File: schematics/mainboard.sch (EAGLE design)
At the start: 146 parts, among them IC1 TEENSY 3.6, IC10 UDN2981A, IC2 LM393, IC3 DRV8835, IC4 LM2596S-ADJ, IC5 LM2596S-5.0, IC6 PCF8574P, IC7 PCF8574P, IC8 LD1117A, IC9 TSOP34830, J1 Servo_1, J10 Uart_5, J11 Servo_3, J12 USB_Host, J13 BNO055, J14 I2C_2, J15 SPI_Display, J16 SPI_2, J17 Uart_6, J18 Maus_select, J19 Erw_analog, J2 Servo_2, J20 Erw_PWM, J21 Erw_GPIO, J22 GY-271, J23 Uart_1, J24 I2C_3, J3 Erw_Pow, J30 H-Bridge Mode, J4 Uart_2, J5 BPS, J6 Erw_ENA, J7 I2C_0, J8 I2C_Display, J9 RPI_SPI0, Q2 IRL3103, SW1 TL36WO, U1 CNY70, U2 BLE-HM-10, U3 BSS138, U4 BSS138, U5 BSS138, X1 Bat

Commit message: Servo PWM pullups corrected, battery voltage divider adjusted
schematic layout improved, signal names unified
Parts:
- J19: device pinhead_ts:PINHD-1X3 -> pinhead_ts:PINHD-1X2
- R1, R37, R38: value 10k -> 4k7
- R2: value 82k -> 100k
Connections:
- net POW4 renamed PWR_SERVO
- net PWM0 renamed PWM1
- net V_BAT_FB renamed BAT_IN_FB
- net +3V3: now also R1.1; no longer R1.2
- net PWM3: now also R1.2; no longer R1.1
- net SERVO3_FB: no longer J19.3
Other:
- note added: "max. 18V Eingangsspannung!"
- note removed: "PWM Pullups erforderlich?"
- moved on the sheet: C16, C17, D3, IC2A, IC2B, J1, J20, R1, R19, R20, R28, R34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

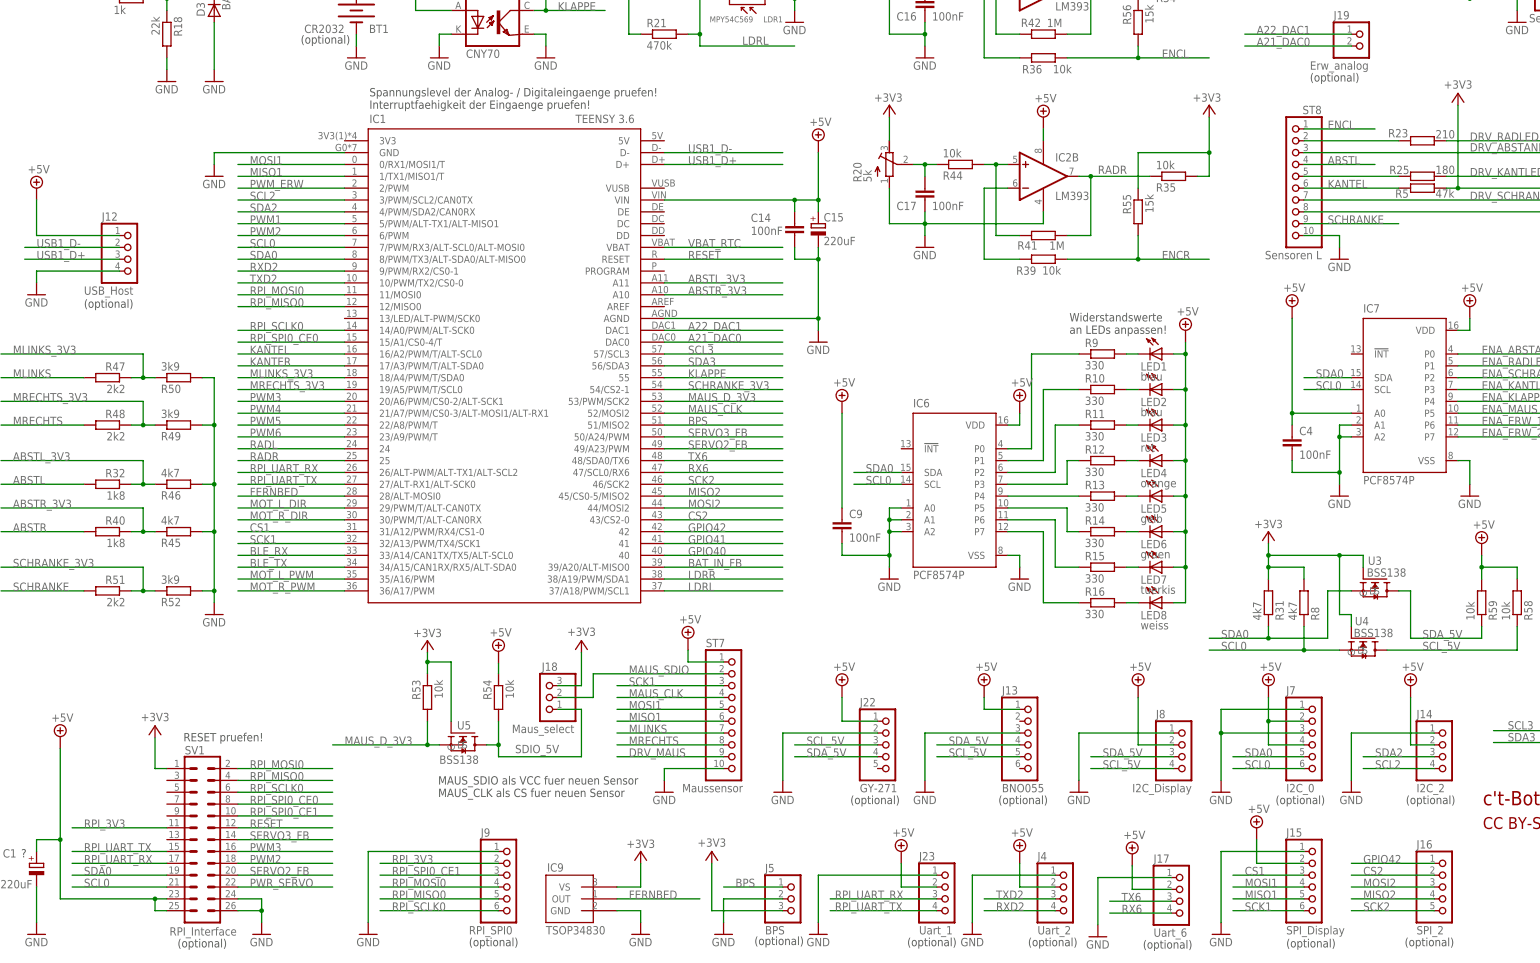
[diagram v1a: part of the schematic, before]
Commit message: bugfix for i2c bus mapping on mainboard
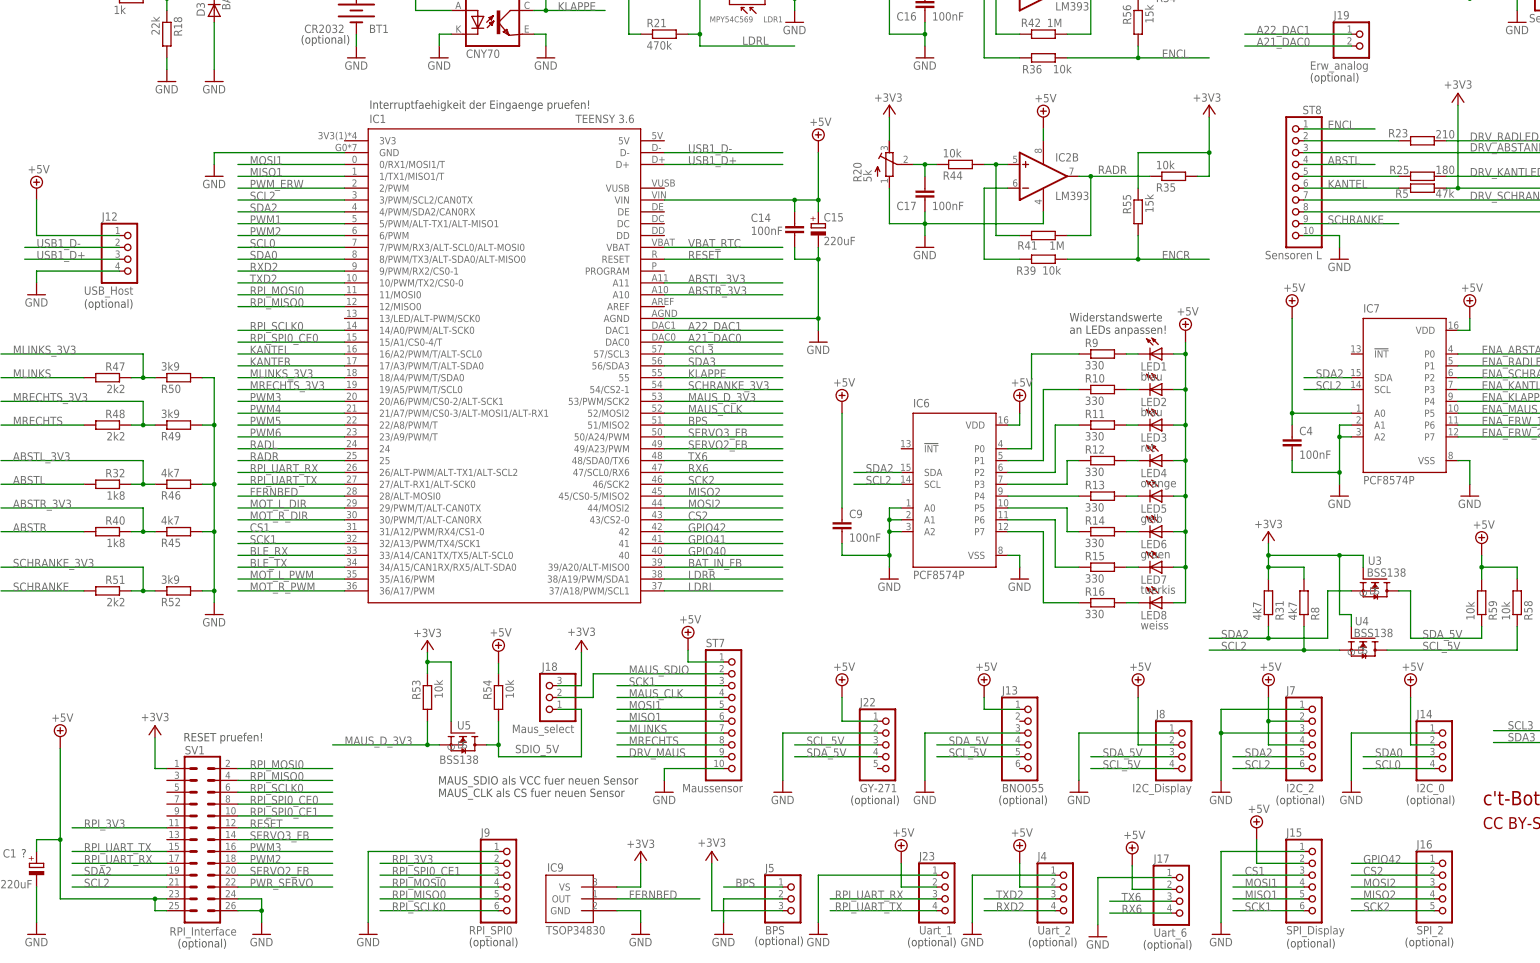
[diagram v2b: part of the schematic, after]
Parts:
- J14: value I2C_2 -> I2C_0
- J7: value I2C_0 -> I2C_2
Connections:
- net SCL0: now also J14.4; no longer IC6.SCL, IC7.SCL, J7.6, R8.1, SV1.21, U4.S
- net SCL2: now also IC6.SCL, IC7.SCL, J7.6, R8.1, SV1.21, U4.S; no longer J14.4
- net SDA0: now also J14.3; no longer IC6.SDA, IC7.SDA, J7.5, R31.1, SV1.19, U3.S
- net SDA2: now also IC6.SDA, IC7.SDA, J7.5, R31.1, SV1.19, U3.S; no longer J14.3
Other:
- note added: "Interruptfaehigkeit der Eingaenge pruefen!"
- note removed: "Spannungslevel der Analog- / Digitaleingaenge pruefen! Interruptfaehigkeit der Eingaenge pruefen!"
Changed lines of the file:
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@@
 <?xml version="1.0" encoding="utf-8"?>
 <!DOCTYPE eagle SYSTEM "eagle.dtd">
-<eagle version="8.6.3">
+<eagle version="8.7.0">
 <drawing>
 <settings>
@@
 <part name="GND20" library="supply1" library_urn="urn:adsk.eagle:library:371" deviceset="GND" device=""/>
 <part name="SUPPLY22" library="supply2_ts" deviceset="+5V" device="" value="+5V"/>
-<part name="J7" library="pinhead_ts" deviceset="PINHD-1X6" device="" value="I2C_0"/>
+<part name="J7" library="pinhead_ts" deviceset="PINHD-1X6" device="" value="I2C_2"/>
 <part name="SUPPLY26" library="supply2_ts" deviceset="+5V" device="" value="+5V"/>
 <part name="GND45" library="supply1" library_urn="urn:adsk.eagle:library:371" deviceset="GND" device=""/>
@@
 <part name="J11" library="pinhead_ts" deviceset="PINHD-1X4" device="" value="Servo_3"/>
 <part name="GND44" library="supply1" library_urn="urn:adsk.eagle:library:371" deviceset="GND" device=""/>
-<part name="J14" library="pinhead_ts" deviceset="PINHD-1X4" device="" value="I2C_2"/>
+<part name="J14" library="pinhead_ts" deviceset="PINHD-1X4" device="" value="I2C_0"/>
 <part name="J15" library="pinhead_ts" deviceset="PINHD-1X6" device="" value="SPI_Display"/>
 <part name="GND46" library="supply1" library_urn="urn:adsk.eagle:library:371" deviceset="GND" device=""/>
@@
 <text x="320.294" y="32.766" size="3.048" layer="94">c't-Bot Hauptplatine v2     !!! UNTESTED DRAFT !!!</text>
 <text x="408.178" y="9.906" size="2.54" layer="94" font="vector">0.2</text>
-<text x="81.534" y="182.118" size="1.778" layer="97">Spannungslevel der Analog- / Digitaleingaenge pruefen!
-Interruptfaehigkeit der Eingaenge pruefen!</text>
+<text x="81.534" y="182.118" size="1.778" layer="97">Interruptfaehigkeit der Eingaenge pruefen!</text>
 <text x="214.63" y="216.408" size="1.778" layer="97">Schaltung checken!
 Widerstandswerte pruefen!</text>
@@
 </segment>
 </net>
-<net name="SDA0" class="0">
+<net name="SDA2" class="0">
 <segment>
 <pinref part="IC7" gate="G$1" pin="SDA"/>
@@
 </segment>
 <segment>
-<pinref part="IC1" gate="G$1" pin="8/PWM/TX3/ALT-SDA0/ALT-MISO0"/>
-<wire x1="76.2" y1="149.86" x2="53.34" y2="149.86" width="0.1524" layer="91"/>
-<label x="55.88" y="149.86" size="1.778" layer="95"/>
+<pinref part="IC1" gate="G$1" pin="4/PWM/SDA2/CAN0RX"/>
+<wire x1="76.2" y1="160.02" x2="53.34" y2="160.02" width="0.1524" layer="91"/>
+<label x="55.88" y="160.02" size="1.778" layer="95"/>
 </segment>
 </net>
-<net name="SCL0" class="0">
+<net name="SCL2" class="0">
 <segment>
 <pinref part="IC7" gate="G$1" pin="SCL"/>
@@
 </segment>
 <segment>
-<pinref part="IC1" gate="G$1" pin="7/PWM/RX3/ALT-SCL0/ALT-MOSI0"/>
-<wire x1="76.2" y1="152.4" x2="53.34" y2="152.4" width="0.1524" layer="91"/>
-<label x="55.88" y="152.4" size="1.778" layer="95"/>
+<pinref part="IC1" gate="G$1" pin="3/PWM/SCL2/CAN0TX"/>
+<wire x1="76.2" y1="162.56" x2="53.34" y2="162.56" width="0.1524" layer="91"/>
+<label x="55.88" y="162.56" size="1.778" layer="95"/>
 </segment>
 </net>
@@
 </segment>
 </net>
-<net name="SCL2" class="0">
-<segment>
-<pinref part="J14" gate="A" pin="4"/>
-<wire x1="294.64" y1="40.64" x2="309.88" y2="40.64" width="0.1524" layer="91"/>
-<label x="297.18" y="40.64" size="1.778" layer="95"/>
-</segment>
-<segment>
-<pinref part="IC1" gate="G$1" pin="3/PWM/SCL2/CAN0TX"/>
-<wire x1="76.2" y1="162.56" x2="53.34" y2="162.56" width="0.1524" layer="91"/>
-<label x="55.88" y="162.56" size="1.778" layer="95"/>
-</segment>
-</net>
-<net name="SDA2" class="0">
-<segment>
-<pinref part="J14" gate="A" pin="3"/>
-<wire x1="294.64" y1="43.18" x2="309.88" y2="43.18" width="0.1524" layer="91"/>
-<label x="297.18" y="43.18" size="1.778" layer="95"/>
-</segment>
-<segment>
-<pinref part="IC1" gate="G$1" pin="4/PWM/SDA2/CAN0RX"/>
-<wire x1="76.2" y1="160.02" x2="53.34" y2="160.02" width="0.1524" layer="91"/>
-<label x="55.88" y="160.02" size="1.778" layer="95"/>
-</segment>
-</net>
 <net name="PWM4" class="0">
 <segment>
@@
 </segment>
 </net>
+<net name="SCL0" class="0">
+<segment>
+<pinref part="IC1" gate="G$1" pin="7/PWM/RX3/ALT-SCL0/ALT-MOSI0"/>
+<wire x1="76.2" y1="152.4" x2="53.34" y2="152.4" width="0.1524" layer="91"/>
+<label x="55.88" y="152.4" size="1.778" layer="95"/>
+</segment>
+<segment>
+<pinref part="J14" gate="A" pin="4"/>
+<wire x1="294.64" y1="40.64" x2="309.88" y2="40.64" width="0.1524" layer="91"/>
+<label x="297.18" y="40.64" size="1.778" layer="95"/>
+</segment>
+</net>
+<net name="SDA0" class="0">
+<segment>
+<pinref part="IC1" gate="G$1" pin="8/PWM/TX3/ALT-SDA0/ALT-MISO0"/>
+<wire x1="76.2" y1="149.86" x2="53.34" y2="149.86" width="0.1524" layer="91"/>
+<label x="55.88" y="149.86" size="1.778" layer="95"/>
+</segment>
+<segment>
+<pinref part="J14" gate="A" pin="3"/>
+<wire x1="294.64" y1="43.18" x2="309.88" y2="43.18" width="0.1524" layer="91"/>
+<label x="297.18" y="43.18" size="1.778" layer="95"/>
+</segment>
+</net>

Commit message: schematics updated to rev 0.3
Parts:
- removed J22: GY-271, pinhead_ts:PINHD-1X5
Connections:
- net RXD2 renamed RX2
- net TXD2 renamed TX2
- net +5V: no longer J22.1
- net GND: no longer J22.2
- net SCL_5V: now also SV1.9; no longer J22.3
- net SDA_5V: now also SV1.7; no longer J22.4
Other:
- note added: "0.3"
- note added: "USB2Bot / WiFi"
- note removed: "0.2"
- moved on the sheet: J13, J14, J24, J7, J8

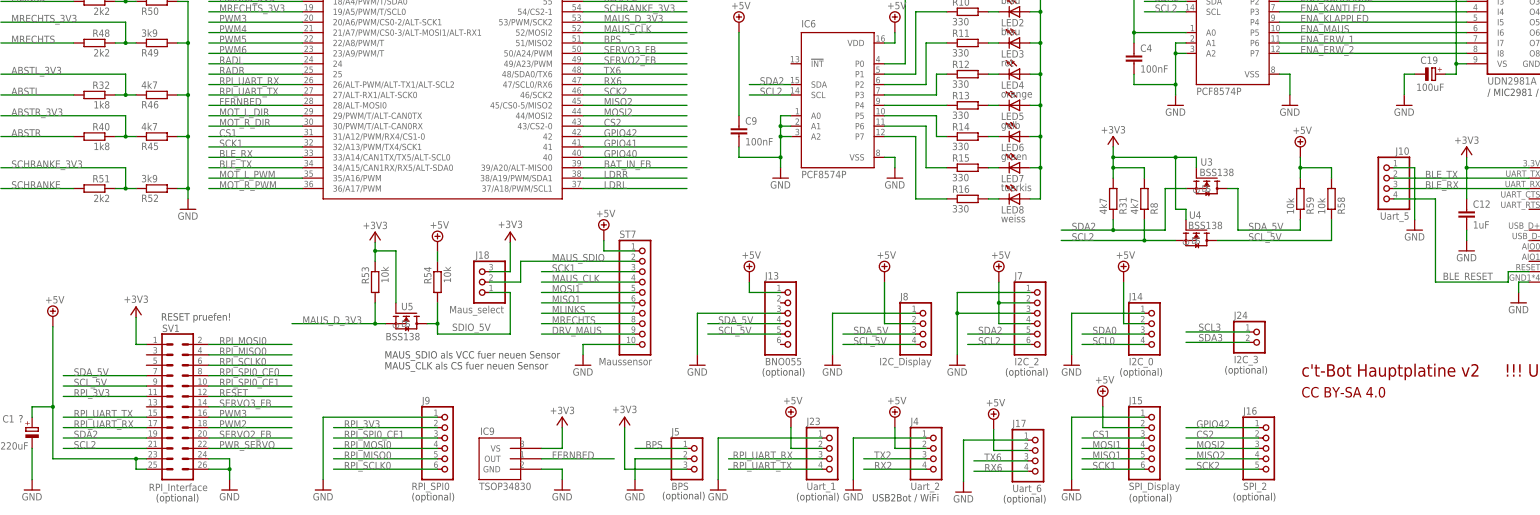
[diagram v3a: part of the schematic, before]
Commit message: mainboard: signal names updated
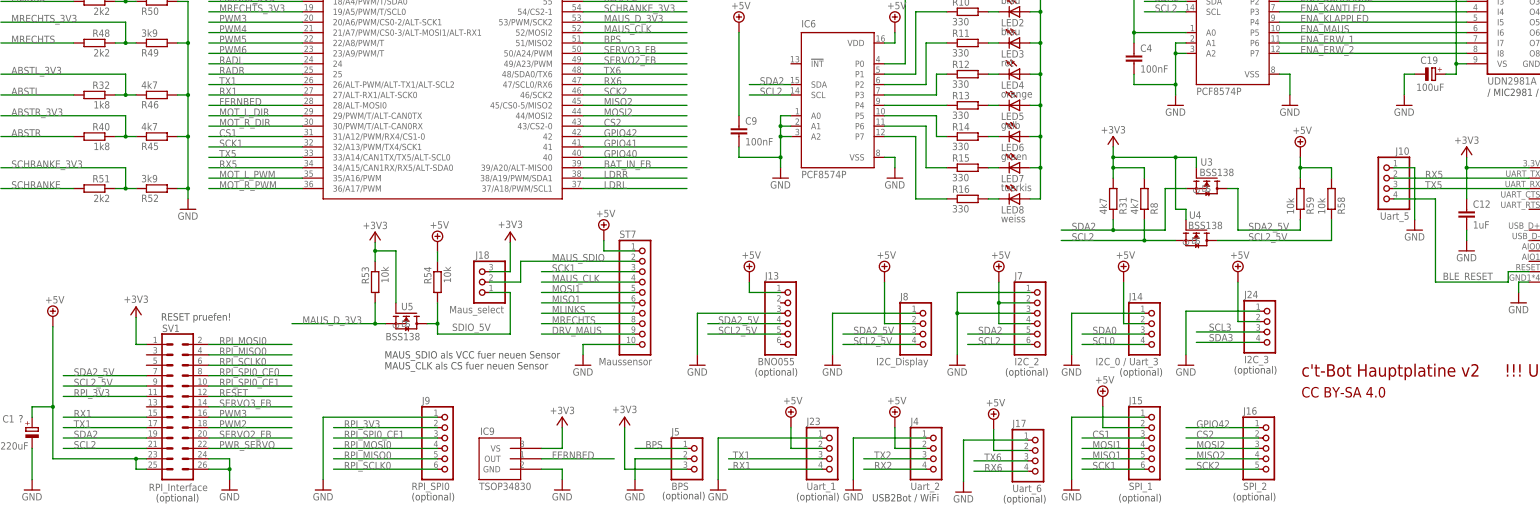
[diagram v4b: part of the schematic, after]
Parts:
- J14: value I2C_0 -> I2C_0 / Uart_3
- J15: value SPI_Display -> SPI_1
- J24: device pinhead_ts:PINHD-1X2 -> pinhead_ts:PINHD-1X4
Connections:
- net BLE_RX renamed TX5
- net BLE_TX renamed RX5
- net RPI_UART_RX renamed TX1
- net RPI_UART_TX renamed RX1
- net SCL_5V renamed SCL2_5V
- net SDA_5V renamed SDA2_5V
- net +5V: now also J24.2
- net GND: now also J24.1
- net SCL3: now also J24.3; no longer J24.1
- net SDA3: now also J24.4; no longer J24.2
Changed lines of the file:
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@@
 <part name="J11" library="pinhead_ts" deviceset="PINHD-1X4" device="" value="Servo_3"/>
 <part name="GND44" library="supply1" library_urn="urn:adsk.eagle:library:371" deviceset="GND" device=""/>
-<part name="J14" library="pinhead_ts" deviceset="PINHD-1X4" device="" value="I2C_0"/>
-<part name="J15" library="pinhead_ts" deviceset="PINHD-1X6" device="" value="SPI_Display"/>
+<part name="J14" library="pinhead_ts" deviceset="PINHD-1X4" device="" value="I2C_0 / Uart_3"/>
+<part name="J15" library="pinhead_ts" deviceset="PINHD-1X6" device="" value="SPI_1"/>
 <part name="GND46" library="supply1" library_urn="urn:adsk.eagle:library:371" deviceset="GND" device=""/>
 <part name="SUPPLY6" library="supply2_ts" deviceset="+5V" device="" value="+5V"/>
@@
 <part name="+3V6" library="supply1_ts" deviceset="+3V3" device=""/>
 <part name="SUPPLY20" library="supply2_ts" deviceset="+5V" device="" value="+5V"/>
-<part name="J24" library="pinhead_ts" deviceset="PINHD-1X2" device="" value="I2C_3"/>
+<part name="J24" library="pinhead_ts" deviceset="PINHD-1X4" device="" value="I2C_3"/>
+<part name="GND47" library="supply1" library_urn="urn:adsk.eagle:library:371" deviceset="GND" device=""/>
+<part name="SUPPLY16" library="supply2_ts" deviceset="+5V" device="" value="+5V"/>
 </parts>
 <sheets>
@@
 <text x="320.294" y="27.686" size="2.54" layer="94">CC BY-SA 4.0</text>
 <text x="395.986" y="48.514" size="1.778" layer="97">(optional)</text>
-<text x="188.468" y="33.02" size="1.778" layer="97">(optional)</text>
+<text x="186.69" y="33.02" size="1.778" layer="97">(optional)</text>
 <text x="20.32" y="139.446" size="1.778" layer="97">(optional)</text>
-<text x="278.13" y="2.286" size="1.778" layer="97">(optional)</text>
+<text x="275.59" y="2.286" size="1.778" layer="97">(optional)</text>
 <text x="66.802" y="196.088" size="1.778" layer="97">(optional)</text>
 <text x="275.844" y="33.02" size="1.778" layer="97">(optional)</text>
@@
 <text x="24.638" y="270.51" size="1.778" layer="97">max. 18V Eingangsspannung!</text>
 <text x="407.416" y="165.354" size="1.778" layer="97">(optional)</text>
-<text x="301.498" y="33.528" size="1.778" layer="97">(optional)</text>
+<text x="303.784" y="33.528" size="1.778" layer="97">(optional)</text>
 </plain>
 <instances>
@@
 <instance part="J8" gate="A" x="228.6" y="43.18" smashed="yes">
 <attribute name="NAME" x="222.25" y="51.435" size="1.778" layer="95"/>
-<attribute name="VALUE" x="217.17" y="35.56" size="1.778" layer="96"/>
+<attribute name="VALUE" x="216.408" y="35.56" size="1.778" layer="96"/>
 </instance>
 <instance part="GND11" gate="1" x="396.24" y="99.06"/>
@@
 </instance>
 <instance part="R33" gate="G$1" x="25.4" y="259.08" rot="MR270"/>
-<instance part="J14" gate="A" x="284.48" y="43.18"/>
+<instance part="J14" gate="A" x="284.48" y="43.18" smashed="yes">
+<attribute name="NAME" x="278.13" y="51.435" size="1.778" layer="95"/>
+<attribute name="VALUE" x="270.002" y="35.56" size="1.778" layer="96"/>
+</instance>
 <instance part="GND46" gate="1" x="264.16" y="35.56"/>
 <instance part="SUPPLY6" gate="+5V" x="276.86" y="58.42"/>
@@
 </instance>
 <instance part="C15" gate="G$1" x="177.8" y="157.48"/>
-<instance part="J13" gate="A" x="195.58" y="45.72"/>
+<instance part="J13" gate="A" x="195.58" y="45.72" smashed="yes">
+<attribute name="NAME" x="189.23" y="56.515" size="1.778" layer="95"/>
+<attribute name="VALUE" x="187.452" y="35.56" size="1.778" layer="96"/>
+</instance>
 <instance part="SUPPLY10" gate="+5V" x="185.42" y="58.42"/>
 <instance part="GND3" gate="1" x="172.72" y="35.56"/>
@@
 </instance>
 <instance part="SUPPLY20" gate="+5V" x="342.9" y="182.88"/>
-<instance part="J24" gate="G$1" x="310.134" y="41.148"/>
+<instance part="J24" gate="A" x="312.674" y="43.688"/>
+<instance part="GND47" gate="1" x="292.1" y="35.56"/>
+<instance part="SUPPLY16" gate="+5V" x="304.8" y="58.42"/>
 </instances>
 <busses>
@@
 <wire x1="342.9" y1="162.56" x2="342.9" y2="180.34" width="0.1524" layer="91"/>
 </segment>
+<segment>
+<pinref part="J24" gate="A" pin="2"/>
+<pinref part="SUPPLY16" gate="+5V" pin="+5V"/>
+<wire x1="310.134" y1="46.228" x2="304.8" y2="46.228" width="0.1524" layer="91"/>
+<wire x1="304.8" y1="46.228" x2="304.8" y2="55.88" width="0.1524" layer="91"/>
+</segment>
 </net>
 <net name="GND" class="0">
@@
 <pinref part="J1" gate="A" pin="1"/>
 <wire x1="327.66" y1="210.82" x2="335.28" y2="210.82" width="0.1524" layer="91"/>
+</segment>
+<segment>
+<pinref part="J24" gate="A" pin="1"/>
+<pinref part="GND47" gate="1" pin="GND"/>
+<wire x1="310.134" y1="48.768" x2="292.1" y2="48.768" width="0.1524" layer="91"/>
+<wire x1="292.1" y1="48.768" x2="292.1" y2="38.1" width="0.1524" layer="91"/>
 </segment>
 </net>
@@
 </segment>
 </net>
-<net name="RPI_UART_TX" class="0">
+<net name="RX1" class="0">
 <segment>
 <pinref part="IC1" gate="G$1" pin="27/ALT-RX1/ALT-SCK0"/>
@@
 </segment>
 </net>
-<net name="RPI_UART_RX" class="0">
+<net name="TX1" class="0">
 <segment>
 <pinref part="IC1" gate="G$1" pin="26/ALT-PWM/ALT-TX1/ALT-SCL2"/>
@@
 </segment>
 <segment>
-<pinref part="J24" gate="G$1" pin="2"/>
-<wire x1="307.594" y1="41.148" x2="292.1" y2="41.148" width="0.1524" layer="91"/>
-<label x="295.148" y="41.402" size="1.778" layer="95"/>
+<label x="297.688" y="41.402" size="1.778" layer="95"/>
+<pinref part="J24" gate="A" pin="4"/>
+<wire x1="310.134" y1="41.148" x2="294.64" y2="41.148" width="0.1524" layer="91"/>
 </segment>
 </net>
@@
 </segment>
 <segment>
-<pinref part="J24" gate="G$1" pin="1"/>
-<wire x1="307.594" y1="43.688" x2="292.1" y2="43.688" width="0.1524" layer="91"/>
-<label x="295.148" y="43.942" size="1.778" layer="95"/>
+<label x="297.688" y="43.942" size="1.778" layer="95"/>
+<pinref part="J24" gate="A" pin="3"/>
+<wire x1="310.134" y1="43.688" x2="294.64" y2="43.688" width="0.1524" layer="91"/>
 </segment>
 </net>
@@
 </segment>
 </net>
-<net name="BLE_TX" class="0">
+<net name="RX5" class="0">
 <segment>
 <pinref part="U2" gate="G$1" pin="UART_TX"/>
@@
 </segment>
 </net>
-<net name="BLE_RX" class="0">
+<net name="TX5" class="0">
 <segment>
 <wire x1="342.9" y1="78.74" x2="375.92" y2="78.74" width="0.1524" layer="91"/>
@@
 </segment>
 </net>
-<net name="SCL_5V" class="0">
+<net name="SCL2_5V" class="0">
 <segment>
 <pinref part="U4" gate="G$1" pin="D"/>
@@
 </segment>
 </net>
-<net name="SDA_5V" class="0">
+<net name="SDA2_5V" class="0">
 <segment>
 <pinref part="J13" gate="A" pin="4"/>
